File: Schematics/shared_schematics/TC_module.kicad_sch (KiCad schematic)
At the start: 10 parts, among them J7 Screw_Terminal_01x02

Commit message: updates and added to cart
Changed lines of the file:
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@@
-	)
-	(junction
-		(at 139.7 90.17)
-		(diameter 0)
-		(color 0 0 0 0)
 	)
 	(junction
@@
 	(wire
 		(pts
-			(xy 139.7 106.68) (xy 139.7 105.41)
-		)
-		(stroke
-			(width 0)
-			(type default)
-		)
-	)
-	(wire
-		(pts
 			(xy 144.78 97.79) (xy 148.59 97.79)
 		)
@@
 	)
 	(symbol
-		(lib_id "power:+3V3")
-		(at 139.7 90.17 270)
+		(lib_id "power:GND")
+		(at 139.7 105.41 270)
 		(unit 1)
 		(exclude_from_sim no)
@@
 		(on_board yes)
 		(dnp no)
-		(property "Reference" "#PWR0117"
-			(at 135.89 90.17 0)
+		(fields_autoplaced yes)
+		(property "Reference" "#PWR0116"
+			(at 133.35 105.41 0)
 			(effects
 				(font
@@
 			)
 		)
-		(property "Value" "+3V3"
-			(at 138.176 88.9 90)
+		(property "Value" "GND"
+			(at 136.3696 105.4099 90)
 			(effects
 				(font
 					(size 1.27 1.27)
 				)
-				(justify left)
+				(justify right)
 			)
 		)
 		(property "Footprint" ""
-			(at 139.7 90.17 0)
+			(at 139.7 105.41 0)
 			(effects
 				(font
@@
 			)
 		)
-		(property "Datasheet" ""
-			(at 139.7 90.17 0)
+		(property "Datasheet" "https://www.ti.com/lit/ds/symlink/drv5055.pdf?HQS=dis-dk-null-digikeymode-dsf-pf-null-wwe&ts=1641231273160"
+			(at 139.7 105.41 0)
 			(effects
 				(font
@@
 			)
 		)
-		(property "Description" "Power symbol creates a global label with name \"+3V3\""
-			(at 139.7 90.17 0)
+		(property "Description" "Hall effect sensor."
+			(at 139.7 105.41 0)
 			(effects
 				(font
-					(size 1.27 1.27)
-				)
-				(hide yes)
-			)
-		)
-		(pin "1"
-		)
-		(instances
-			(project "upper_lc_board"
-				(path "/9b1a1d2a-fad7-4f10-83f3-1f83e9656c75/03f1622b-3dda-4e29-911f-7cc762ec6c20/911e7585-9a9d-4803-9ce9-9fc1f19be4ae"
-					(reference "#PWR0117")
-					(unit 1)
-				)
-			)
-			(project "lower_lc_board"
-				(path "/d63798c4-e363-437e-9012-e4aff32e6642/c6419db7-28a9-4bfa-8244-fc88166c795c/0f673b05-1261-4d55-8b13-e3d5496cfefa"
-					(reference "#PWR0118")
-					(unit 1)
-				)
-			)
-		)
-	)
-	(symbol
-		(lib_id "power:GND")
-		(at 139.7 106.68 270)
-		(unit 1)
-		(exclude_from_sim no)
-		(in_bom yes)
-		(on_board yes)
-		(dnp no)
-		(fields_autoplaced yes)
-		(property "Reference" "#PWR0116"
-			(at 133.35 106.68 0)
-			(effects
-				(font
-					(size 1.27 1.27)
-				)
-				(hide yes)
-			)
-		)
-		(property "Value" "GND"
-			(at 136.3696 106.6799 90)
-			(effects
-				(font
-					(size 1.27 1.27)
-				)
-				(justify right)
-			)
-		)
-		(property "Footprint" ""
-			(at 139.7 106.68 0)
-			(effects
-				(font
-					(size 1.27 1.27)
-				)
-				(hide yes)
-			)
-		)
-		(property "Datasheet" "https://www.ti.com/lit/ds/symlink/drv5055.pdf?HQS=dis-dk-null-digikeymode-dsf-pf-null-wwe&ts=1641231273160"
-			(at 139.7 106.68 0)
-			(effects
-				(font
-					(size 1.27 1.27)
-				)
-				(hide yes)
-			)
-		)
-		(property "Description" "Hall effect sensor."
-			(at 139.7 106.68 0)
-			(effects
-				(font

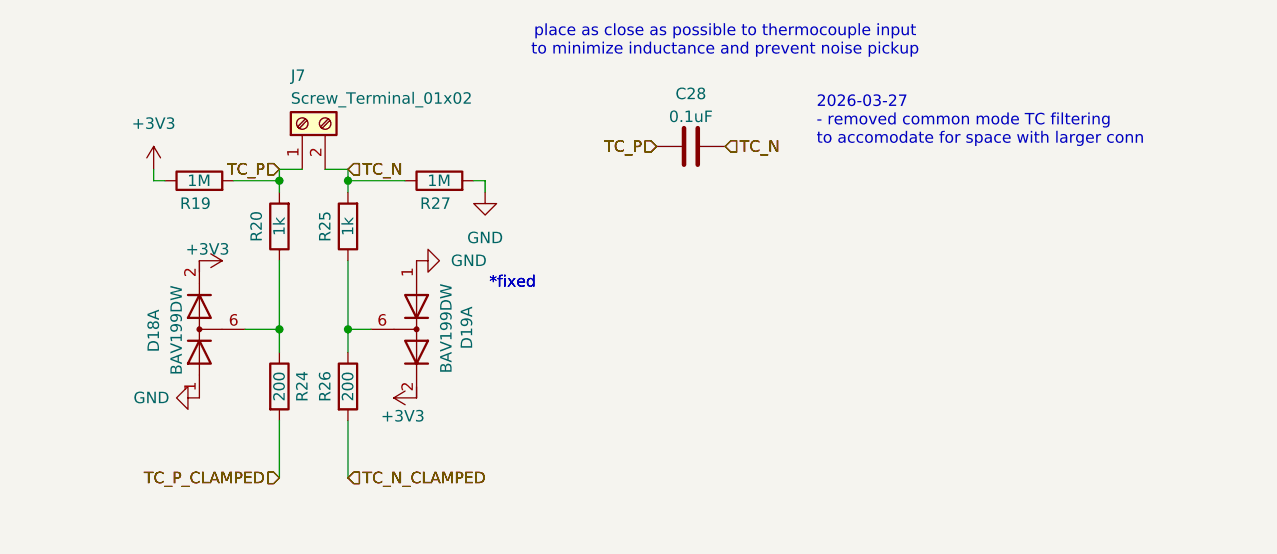
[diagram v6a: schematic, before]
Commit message: replace old part number, clean up old design comments
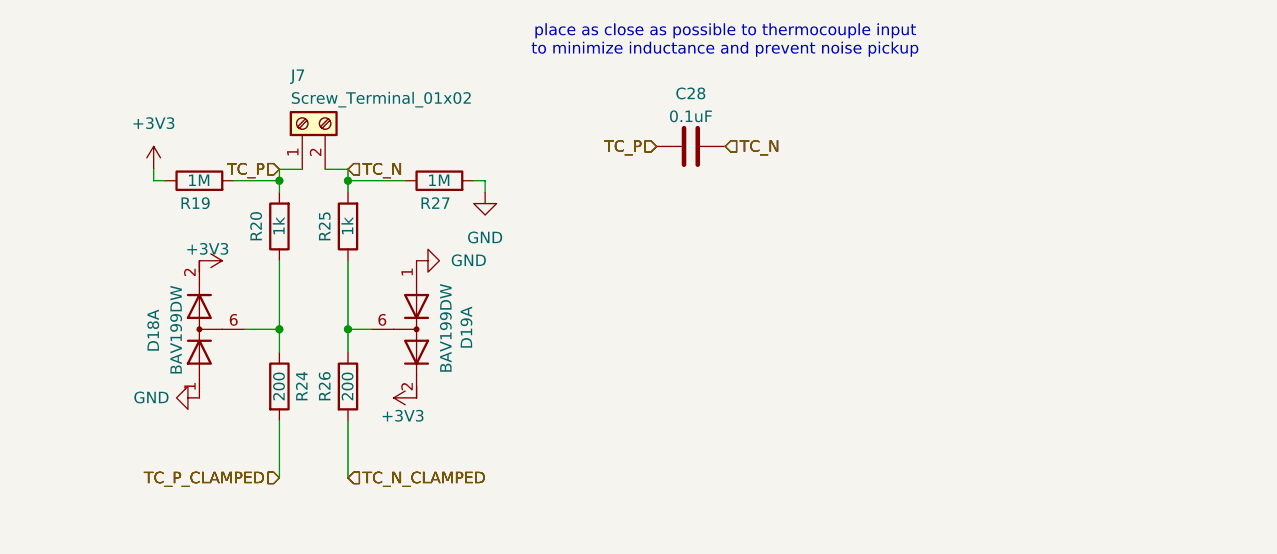
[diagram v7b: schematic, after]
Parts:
- J7: Digikey 277-1734-ND -> A98333-ND
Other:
- note removed: "*fixed"
- note removed: "2026-03-27 - removed common mode TC filtering to accomodate for space with larger conn"
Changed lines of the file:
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@@
-		)
-	)
-	(text "2026-03-27\n- removed common mode TC filtering\nto accomodate for space with larger conn"
-		(exclude_from_sim no)
-		(at 208.28 74.676 0)
-		(effects
-			(font
-				(size 1.27 1.27)
-			)
-			(justify left)
-		)
-	)
-	(text "*fixed\n"
-		(exclude_from_sim no)
-		(at 174.498 92.71 0)
-		(effects
-			(font
-				(size 1.27 1.27)
-			)
-		)
-	)
-	(text "*fixed\n"
-		(exclude_from_sim no)
-		(at 174.498 92.71 0)
-		(effects
-			(font
-				(size 1.27 1.27)
-			)
 		)
 	)
@@
 			)
 		)
-		(property "Digikey" "277-1734-ND"
+		(property "Digikey" "A98333-ND"
 			(at 151.13 74.93 90)
 			(effects

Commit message: add board-specifc READMEs (TODO), cleanup schematic titles
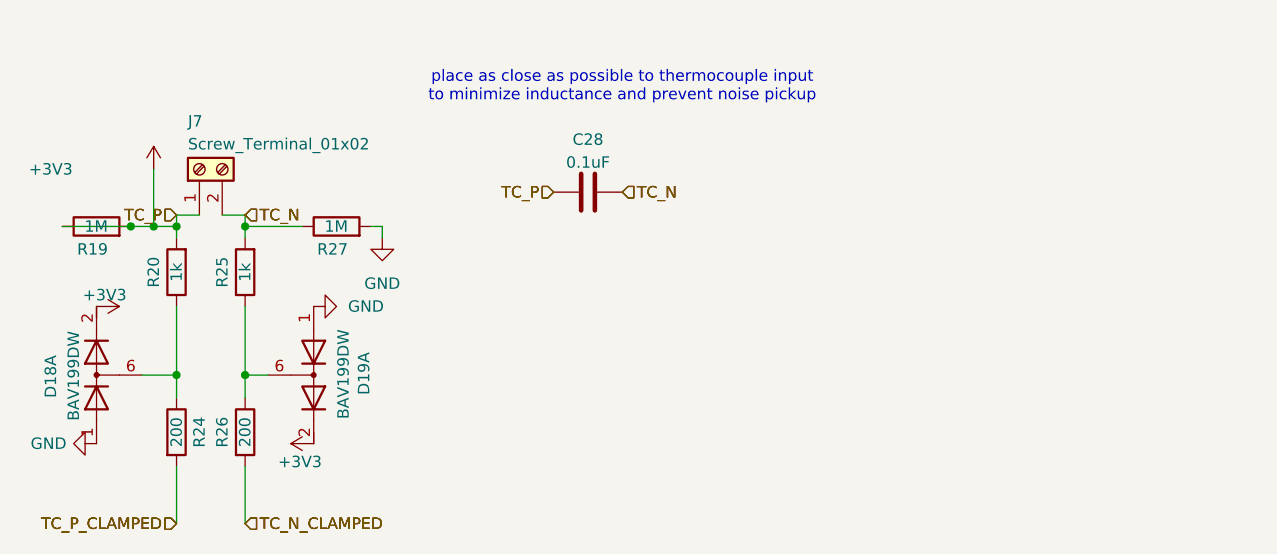
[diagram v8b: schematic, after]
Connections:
- net TC_P is gone; now on net +3V3: C28.2, J7.1 (Pin_1), R19.2, R20.2
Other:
- moved on the sheet: C28, D18A, D19A, J7, R19, R20, R24, R25, R26, R27
